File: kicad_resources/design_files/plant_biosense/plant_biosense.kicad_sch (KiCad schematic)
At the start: 71 parts, among them J1 RJ45_Shielded, J2 RJ45_Shielded, U1 CD4051B, U10 TXS0108EPW, U11 OP07, U12 TL081, U13 NodeMCU1.0(ESP-12E), U14 ADS1115IDGS, U2 CD4051B, U3 2S4P LI-ION BATTERY, U4 2S LI-ION BMS 10A, U5 2S LI-ION CC/CV CHARGER, U6 XL4015, U7 AD620_instrumentation_amplifi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, U8 INA219AxD, U9 OP07

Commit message: Update plant biosense schematic and PDF
Revise the schematic wiring and component references, assign additional nets to their classes, and refresh the exported CEREPHYTE 4.5 PDF.
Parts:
- renumbered C14 to C10, C9 to C11, C11 to C12, C12 to C13, C13 to C14, C10 to C9, U3 to U1, U4 to U2, U5 to U3, U1 to U4, U2 to U5, U8 to U7, U7 to U8
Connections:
- net arduino5v: now also C22.1, C25.1, U13.15 (VIN)
- net vdd: no longer C22.1, C25.1, U13.15 (VIN)

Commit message: Update CEREPHYTE 4.5 schematic
Refresh the schematic PDF and update KiCad netclass assignments, including Power_Lines flags. Remove the BP+ label and its wire from the schematic.
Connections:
- net BP+: no longer U6.1 (IN+), U7.7 (IN-)
- new net: U6.1 (IN+), U7.7 (IN-)
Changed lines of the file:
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@@
 	(title_block
 		(title "CEREPHYTE\n")
-		(date "2026-10-16")
+		(date "2026-10-21")
 		(rev "4.5")
 		(company "ISLERI")
@@
 	)
 	(junction
-		(at 60.96 124.46)
-		(diameter 0)
-		(color 0 0 0 0)
-	)
-	(junction
 		(at 139.7 33.02)
 		(diameter 0)
@@
 	(wire
 		(pts
-			(xy 60.96 120.65) (xy 60.96 124.46)
-		)
-		(stroke
-			(width 0)
-			(type default)
-		)
-	)
-	(wire
-		(pts
 			(xy 26.67 92.71) (xy 31.75 92.71)
 		)
@@
 		)
 	)
-	(label "BP+"
-		(at 60.96 120.65 180)
-		(effects
-			(font
-				(size 1.27 1.27)
-			)
-			(justify right bottom)
-		)
-	)
 	(label "INH2"
 		(at 157.48 101.6 0)
@@
 	(netclass_flag ""
 		(length 2.54)
+		(shape dot)
+		(at 59.69 124.46 0)
+		(fields_autoplaced yes)
+		(effects
+			(font
+				(size 1.27 1.27)
+			)
+			(justify left bottom)
+		)
+		(property "Net Class" "Power_Lines"
+			(at 60.3885 121.92 0)
+			(hide yes)
+			(show_name no)
+			(do_not_autoplace no)
+			(effects
+				(font
+					(size 1.27 1.27)
+				)
+				(justify left)
+			)
+		)
+		(property "Component Class" ""
+			(at -3.81 -8.89 0)
+			(show_name no)
+			(do_not_autoplace no)
+			(effects
+				(font
+					(size 1.27 1.27)
+					(italic yes)
+				)
+			)
+		)
+	)
+	(netclass_flag ""
+		(length 2.54)
 		(shape round)
 		(at 133.35 92.71 180)
@@
 			(show_name no)
 			(do_not_autoplace no)
+			(effects
+				(font
+					(size 1.27 1.27)
+					(italic yes)
+				)
+			)
+		)
+	)
+	(netclass_flag ""
+		(length 2.54)
+		(shape dot)
+		(at 66.04 146.05 0)
+		(fields_autoplaced yes)
+		(effects
+			(font
+				(size 1.27 1.27)
+			)
+			(justify left bottom)
+		)
+		(property "Net Class" "Power_Lines"
+			(at 66.7385 143.51 0)
+			(hide yes)
+			(show_name no)
+			(do_not_autoplace no)
+			(effects
+				(font
+					(size 1.27 1.27)
+				)
+				(justify left)
+			)
+		)
+		(property "Component Class" ""
+			(at 2.54 12.7 0)
+			(show_name no)
+			(do_not_autoplace no)

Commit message: Update plant biosense schematic power labels
Replace Arduino-specific power labels with VDD, correct I/O labels and connections, and update no-connect markers. Record the schematic designators and refresh the CEREPHYTE 4.5 PDF.
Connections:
- net IO1: now also A1.11 (A2); no longer U10.17 (B3)
- net IO2: now also A1.12 (A3); no longer U10.16 (B4)
- net vdd: now also C22.1, C23.1, C24.1, C25.1, MAX1.8 (vcc), U10.19 (VCCB), U13.15 (VIN), U14.8 (VDD)
- net IOO1: no longer names the net of U10.4 (A3)
- net IOO1: no longer U13.27 (D3(GPIO0))
- net IOO2: no longer names the net of U10.5 (A4)
- net IOO2: no longer U13.26 (D4(GPIO2))
- removed net arduino5v: A1.5 (+5V), C22.1, C23.1, C24.1, C25.1, MAX1.8 (vcc), U10.19 (VCCB), U13.15 (VIN), U14.8 (VDD)
- no-connect marks 41 -> 46
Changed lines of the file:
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@@
 	)
 	(no_connect
+		(at 279.4 81.28)
+	)
+	(no_connect
 		(at 279.4 93.98)
 	)
@@
 	)
 	(no_connect
+		(at 203.2 87.63)
+	)
+	(no_connect
 		(at 223.52 92.71)
 	)
@@
 	)
 	(no_connect
-		(at 190.5 99.06)
-	)
-	(no_connect
 		(at 274.32 153.67)
 	)
@@
 	)
 	(no_connect
+		(at 203.2 90.17)
+	)
+	(no_connect
+		(at 223.52 90.17)
+	)
+	(no_connect
 		(at 223.52 95.25)
 	)
@@
 	)
 	(no_connect
+		(at 279.4 83.82)
+	)
+	(no_connect
 		(at 238.76 78.74)
 	)
@@
 	)
 	(no_connect
+		(at 223.52 87.63)
+	)
+	(no_connect
 		(at 254 153.67)
 	)
@@
 	)
 	(no_connect
+		(at 182.88 68.58)
+	)
+	(no_connect
 		(at 190.5 88.9)
 	)
@@
 	)
 	(no_connect
-		(at 190.5 101.6)
-	)
-	(no_connect
 		(at 279.4 99.06)
 	)
@@
 	(wire
 		(pts
+			(xy 127 110.49) (xy 130.81 110.49)
+		)
+		(stroke
+			(width 0)
+			(type default)
+		)
+	)
+	(wire
+		(pts
 			(xy 168.91 44.45) (xy 184.15 44.45)
 		)
@@
 	(wire
 		(pts
-			(xy 182.88 64.77) (xy 182.88 68.58)
-		)
-		(stroke
-			(width 0)
-			(type default)
-		)
-	)
-	(wire
-		(pts
 			(xy 97.79 12.7) (xy 97.79 19.05)
 		)
@@
 		)
 	)
-	(label "arduino5v"
-		(at 130.81 110.49 180)
-		(effects
-			(font
-				(size 1.27 1.27)
-				(thickness 0.1588)
-			)
-			(justify right bottom)
-		)
-	)
 	(label "LSDA"
 		(at 279.4 78.74 0)
@@
 		)
 	)
-	(label "IOO1"
-		(at 203.2 87.63 180)
-		(effects
-			(font
-				(size 1.27 1.27)
-			)
-			(justify right bottom)
-		)
-	)
 	(label "IO1"
-		(at 223.52 87.63 0)
+		(at 190.5 99.06 0)
 		(effects
 			(font
@@
 	)
 	(label "IO2"
-		(at 223.52 90.17 0)
+		(at 190.5 101.6 0)
+		(effects
+			(font
+				(size 1.27 1.27)
+			)
+			(justify left bottom)
+		)
+	)
+	(label "vdd"
+		(at 227.33 113.03 0)
 		(effects
 			(font
@@
 		)
 	)
-	(label "IOO1"
-		(at 279.4 81.28 0)
-		(effects
-			(font
-				(size 1.27 1.27)
-			)
-			(justify left bottom)
-		)
-	)
 	(label "b1"
 		(at 157.48 86.36 0)
@@
 		)
 	)
-	(label "arduino5v"
-		(at 215.9 72.39 0)
+	(label "a1"
+		(at 157.48 83.82 0)
 		(effects
 			(font
 				(size 1.27 1.27)
-				(thickness 0.1588)
 			)
 			(justify left bottom)
 		)
 	)
-	(label "a1"
-		(at 157.48 83.82 0)
+	(label "vdd"
+		(at 215.9 72.39 0)
 		(effects
 			(font
@@
 		)
 	)
-	(label "arduino5v"
-		(at 182.88 64.77 0)
-		(effects
-			(font
-				(size 1.27 1.27)
-				(thickness 0.1588)
-			)
-			(justify left bottom)
-		)
-	)
 	(label "m0"
 		(at 46.99 29.21 0)
@@
 		)
 	)
-	(label "IOO2"
-		(at 279.4 83.82 0)
-		(effects
-			(font
-				(size 1.27 1.27)
-			)
-			(justify left bottom)
-		)
-	)
 	(label "m3"
 		(at 46.99 77.47 0)
@@
 		)
 	)
-	(label "IOO2"
-		(at 203.2 90.17 180)
-		(effects
-			(font
-				(size 1.27 1.27)
-			)
-			(justify right bottom)
-		)
-	)
 	(label "m5"
 		(at 44.45 177.8 0)
@@
 		)
 	)
+	(label "vdd"
+		(at 264.16 129.54 0)
+		(effects
+			(font
+				(size 1.27 1.27)
+			)
+			(justify left bottom)
+		)
+	)
 	(label "m2"
 		(at 46.99 34.29 0)
@@
 		)
 	)
-	(label "arduino5v"
-		(at 227.33 113.03 0)
-		(effects
-			(font
-				(size 1.27 1.27)
-				(thickness 0.1588)
-			)
-			(justify left bottom)
-		)
-	)
 	(label "vdd"
 		(at 74.93 64.77 0)
@@
 		)
 	)
-	(label "arduino5v"
-		(at 264.16 129.54 0)
-		(effects
-			(font
-				(size 1.27 1.27)
-				(thickness 0.1588)
-			)
-			(justify left bottom)
-		)
-	)
 	(label "INASCL"
 		(at 223.52 100.33 0)
@@
 		(effects
 			(font
+				(size 1.27 1.27)
+			)
+			(justify left bottom)
+		)
+	)
+	(label "vdd"
+		(at 127 110.49 0)
+		(effects
+			(font

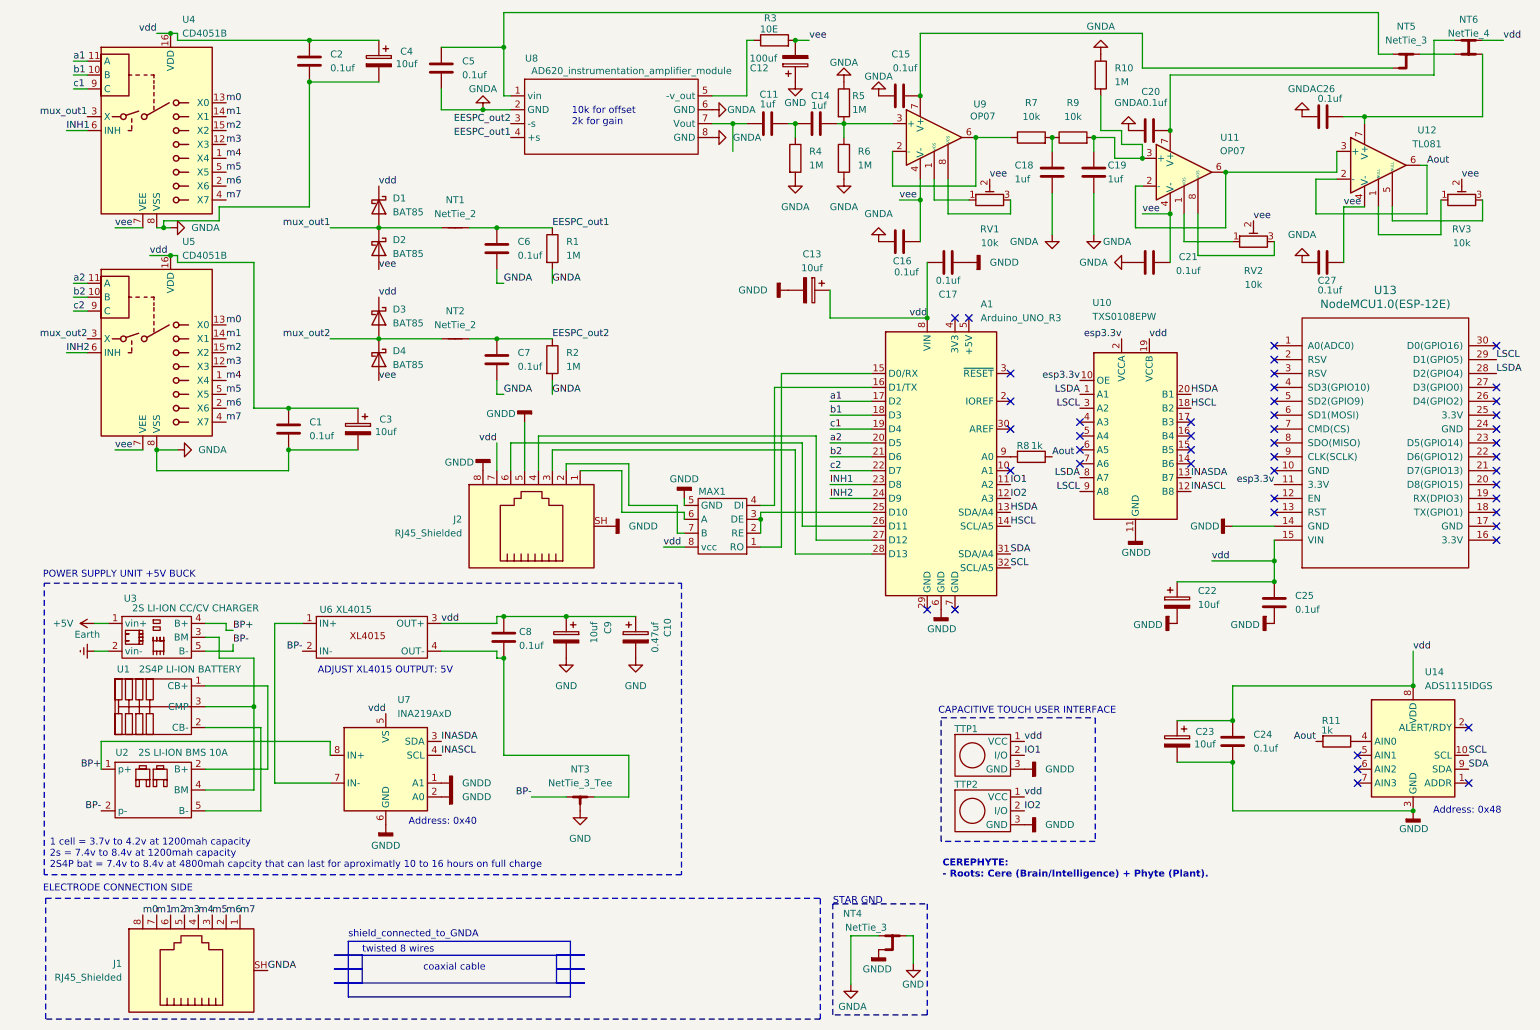
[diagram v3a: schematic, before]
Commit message: Add CEREPHYTE v5 schematic
Update the KiCad design to revision 5 with revised component placement and signal wiring, add the v5 PDF, and standardize versioned schematic filenames.
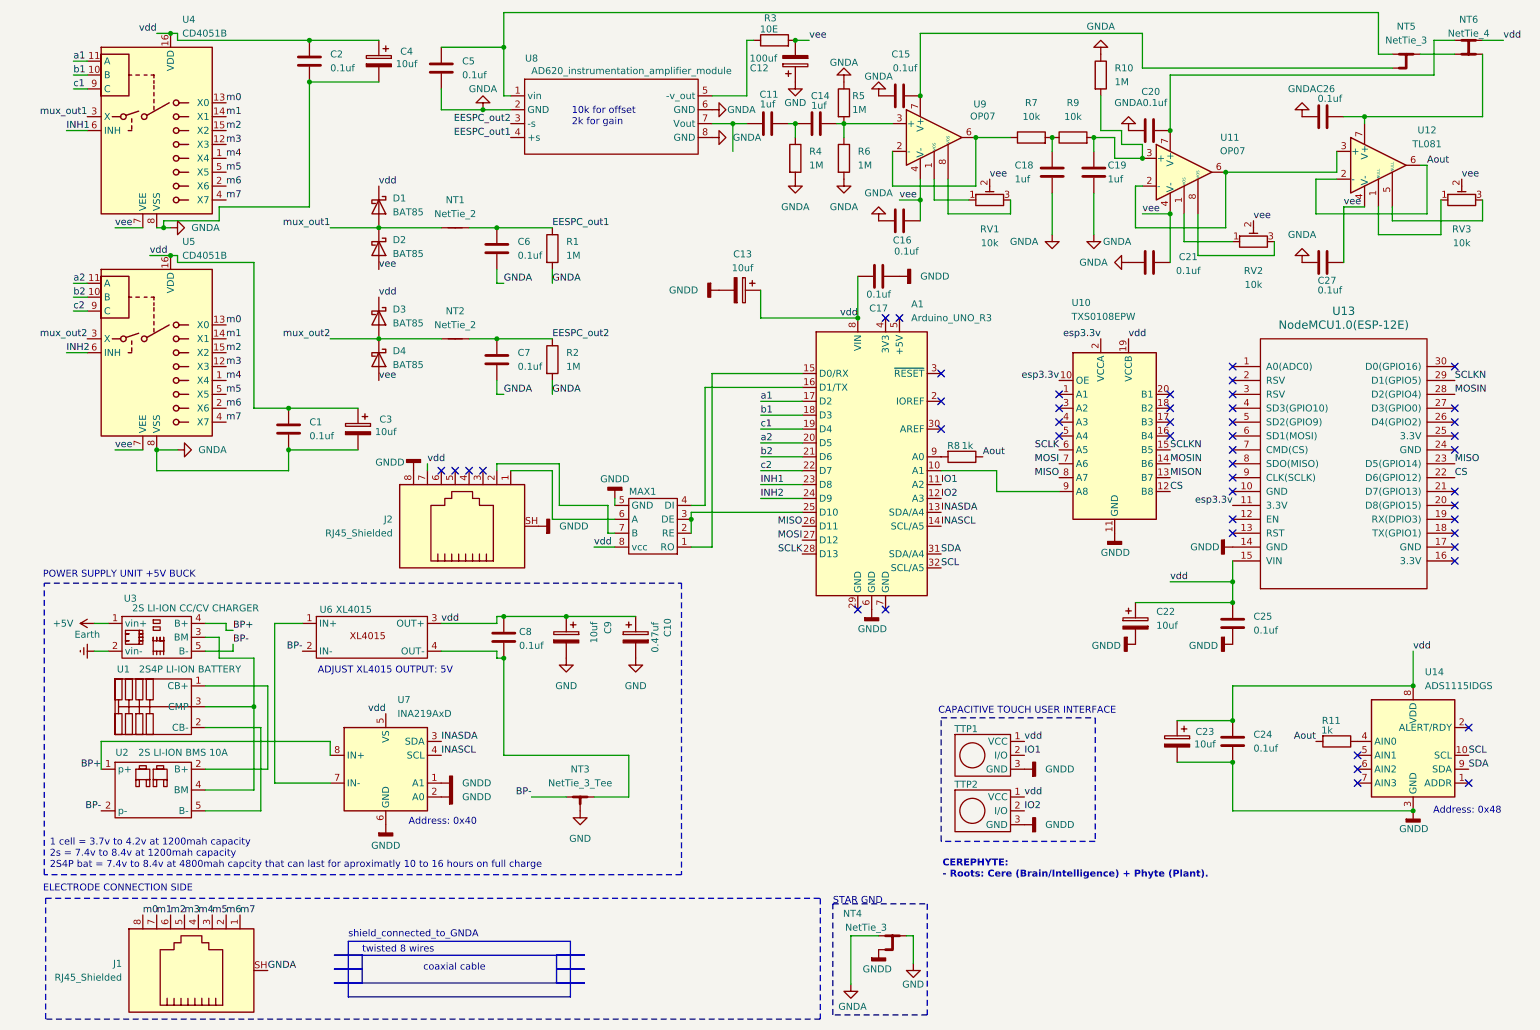
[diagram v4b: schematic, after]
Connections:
- net GNDD: no longer J2.5
- net INASCL: now also A1.14 (SCL/A5); no longer U10.12 (B8)
- net INASDA: now also A1.13 (SDA/A4); no longer U10.13 (B7)
- net at A1.10 (A1): now also U10.9 (A8)
- net at J2.6: no longer A1.26 (D11)
- net at J2.4: no longer A1.27 (D12)
- net at J2.3: no longer A1.28 (D13)
- net MOSIN: now reaches U10.14 (B6)
- net MOSIN: now also U13.28 (D2(GPIO4))
- net SCLKN: now reaches U10.15 (B5)
- net SCLKN: now also U13.29 (D1(GPIO5))
- net SCLK: now reaches U10.6 (A5)
- net SCLK: now also A1.28 (D13)
- net MOSI: now reaches U10.7 (A6)
- net MOSI: now also A1.27 (D12)
- net CS: now reaches U13.22 (D6(GPIO12))
- net CS: now also U10.12 (B8)
- net MISO: now reaches U13.23 (D5(GPIO14))
- net MISO: now also A1.26 (D11), U10.8 (A7)
- net HSCL: no longer names the net of U10.18 (B2)
- net HSCL: no longer A1.14 (SCL/A5)
- net HSDA: no longer names the net of U10.20 (B1)
- net HSDA: no longer A1.13 (SDA/A4)
- removed net LSCL: U10.3 (A2), U10.9 (A8), U13.29 (D1(GPIO5))
- removed net LSDA: U10.1 (A1), U10.8 (A7), U13.28 (D2(GPIO4))
- new net MISON: U10.13 (B7)
- no-connect marks 46 -> 47
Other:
- moved on the sheet: A1, C13, C16, C17, C22, C25, J2, MAX1, R8, U10, U13

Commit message: Update CEREPHYTE rev 5 schematic
Revise SPI signal labels and connections, update component annotations and project metadata, and regenerate the schematic PDF. Ignore KiCad history files.
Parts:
- renumbered C13 to C11, C11 to C12, C12 to C13, C17 to C15, C15 to C16, C16 to C17, C22 to C20, C20 to C21, C21 to C22, C25 to C24, C24 to C25, R8 to R7, R7 to R8, U13 to U12, U12 to U13
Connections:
- net at A1.10 (A1): no longer U10.9 (A8)
- net CS: no longer names the net of U10.12 (B8)
- net CS: no longer U12.22 (D6(GPIO12))
- net MISO renamed SS_TX_A
- net SS_TX_A: no longer U12.23 (D5(GPIO14))
- net MISON renamed SS_RX_ESP
- net SS_RX_ESP: now also U12.23 (D5(GPIO14))
- net MOSI renamed SS_RX_A
- net MOSIN renamed SS_TX_ESP
- net SCLK: no longer names the net of A1.28 (D13)
- net SCLK: no longer U10.6 (A5)
- net SCLKN: no longer names the net of U10.15 (B5)
- net SCLKN: no longer U12.29 (D1(GPIO5))
- no-connect marks 47 -> 55
